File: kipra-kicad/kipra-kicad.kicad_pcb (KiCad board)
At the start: 2 copper layers, 128.2 x 134.8 mm, 51 parts

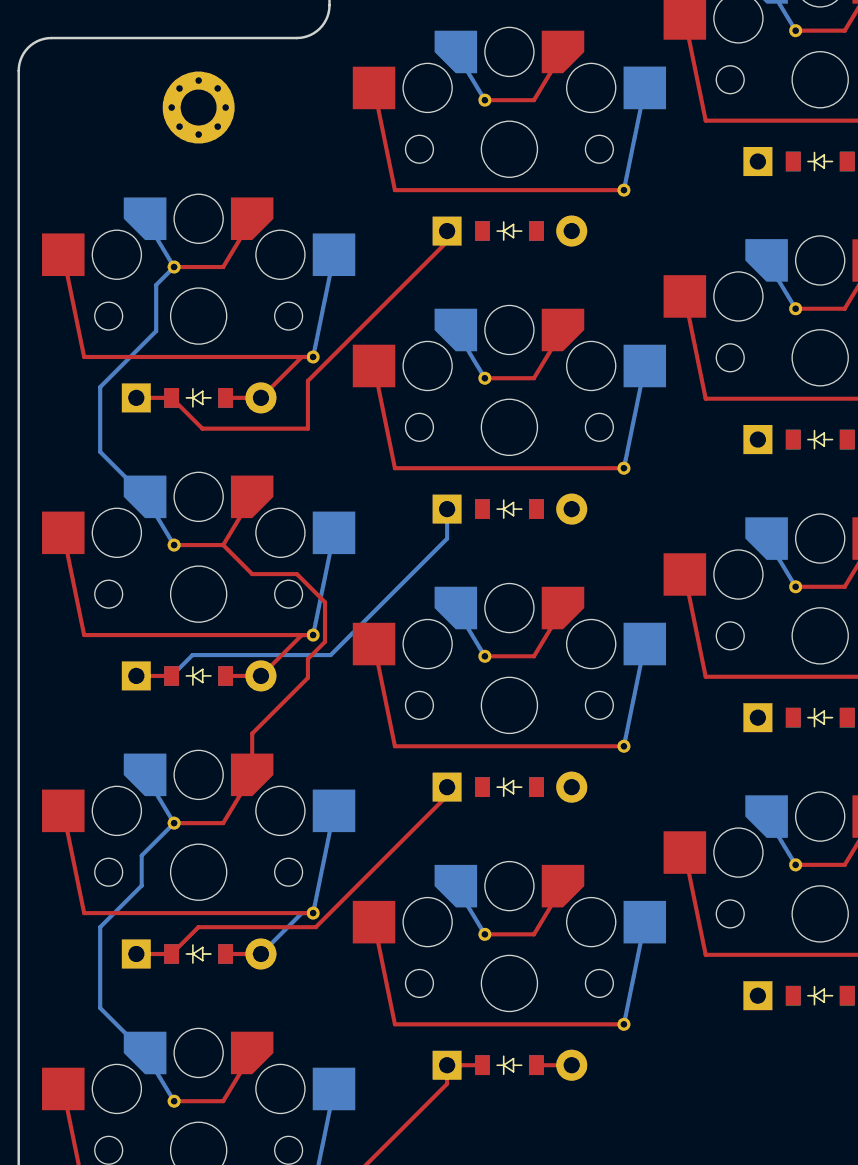
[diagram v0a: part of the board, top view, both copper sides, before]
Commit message: route traces up ring column
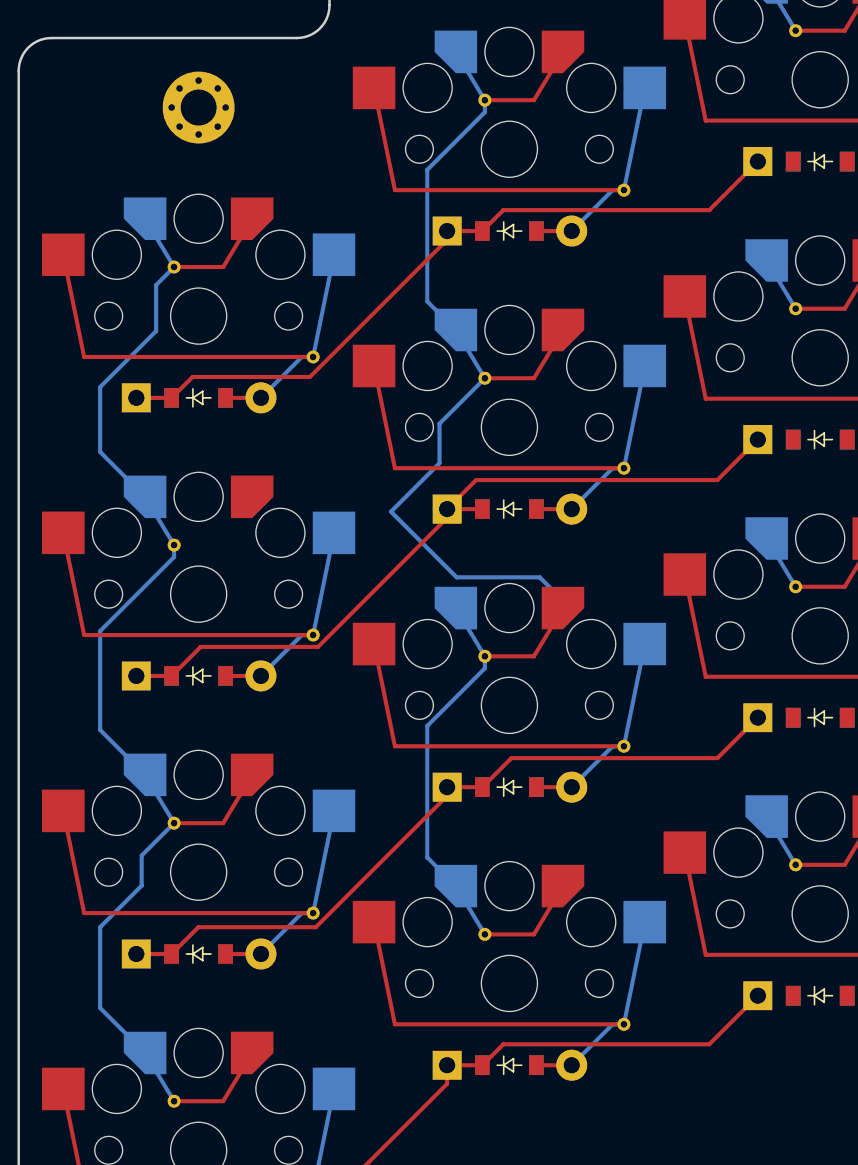
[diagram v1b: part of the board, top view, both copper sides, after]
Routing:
- net P16: track 49.7 -> 105.0 mm
- net P06: track 24.3 -> 46.5 mm
- net P07: track 23.5 -> 44.3 mm
- net P08: track 26.1 -> 44.7 mm
- net P05: track 26.9 -> 44.3 mm
- net P10: track 103.9 -> 94.5 mm
- net ring_two: track 26.8 -> 33.1 mm
- net ring_three: track 26.8 -> 33.1 mm
- net ring_four: track 26.8 -> 33.1 mm
- net ring_one: track 28.9 -> 33.1 mm
- net pinky_three: track 33.1 -> 33.8 mm
- net pinky_four: track 33.1 -> 33.8 mm

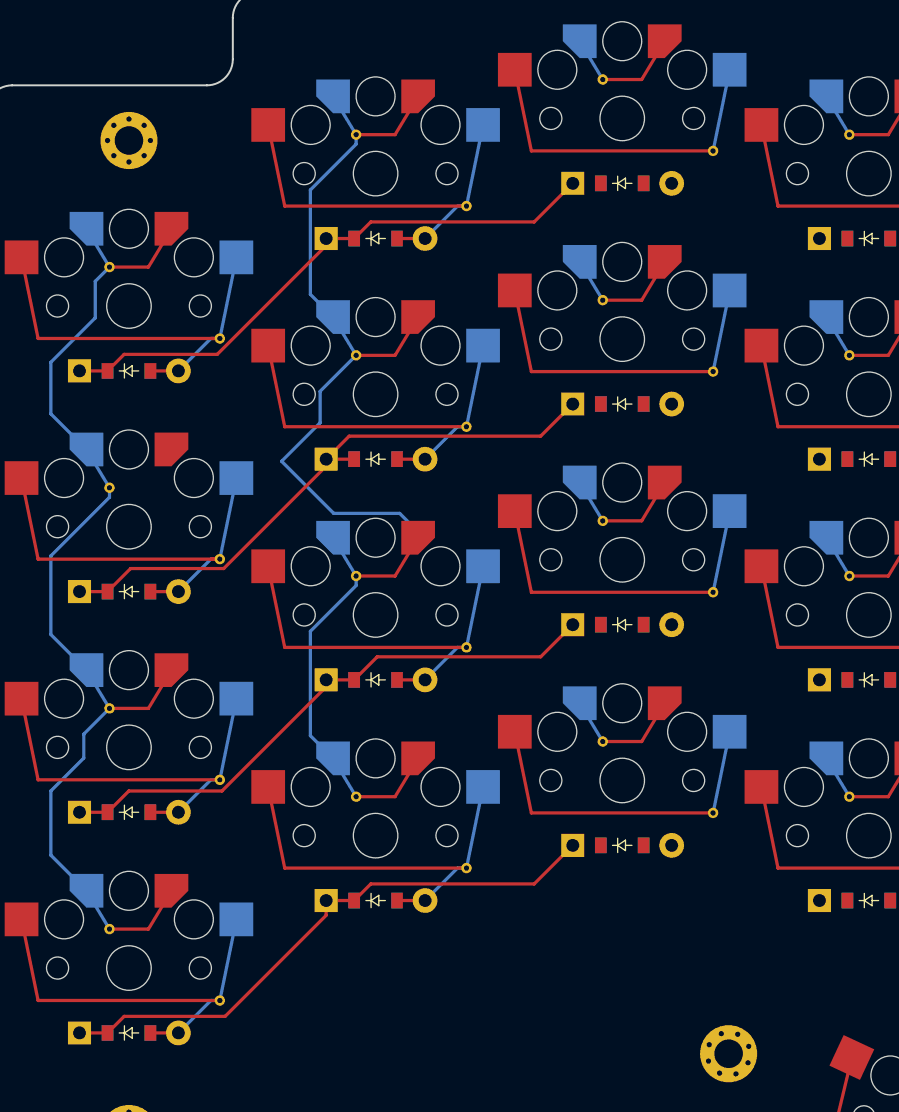
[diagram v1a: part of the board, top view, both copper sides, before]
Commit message: route traces up middle column
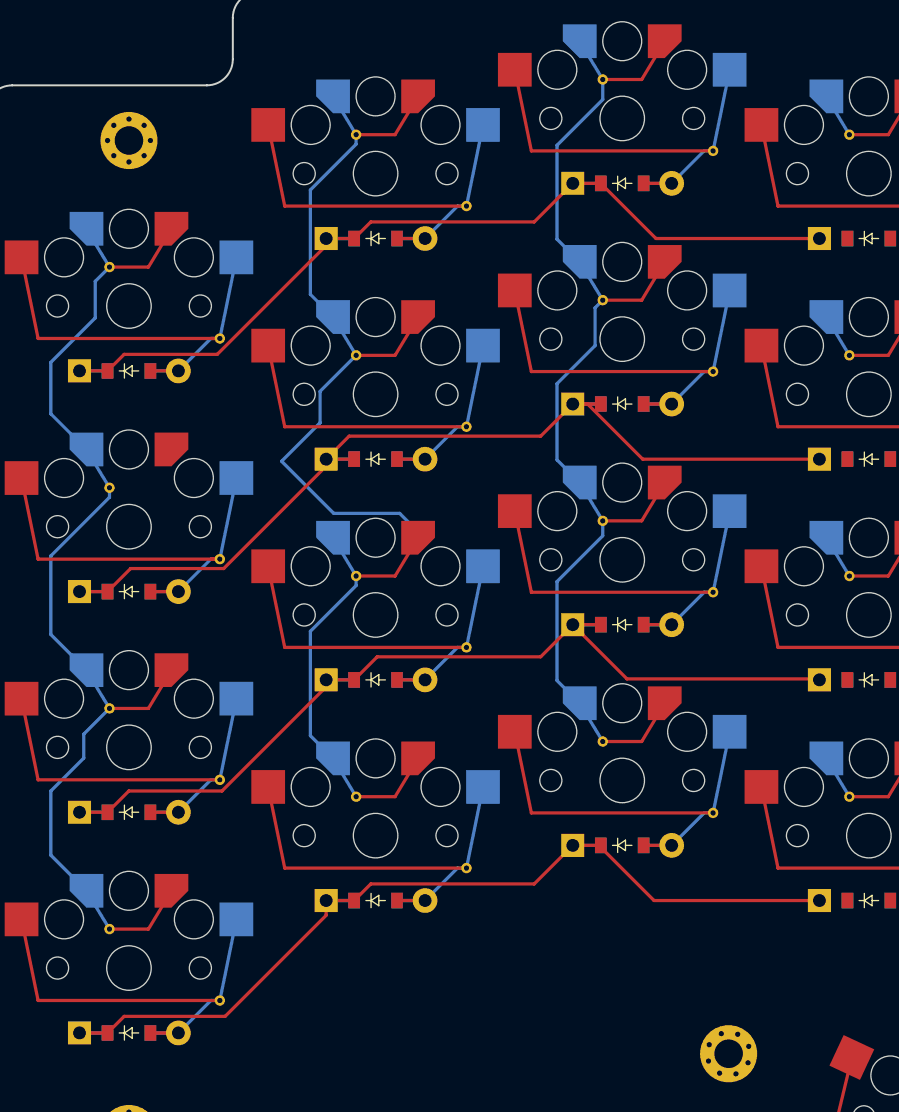
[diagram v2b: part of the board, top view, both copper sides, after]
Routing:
- net P14: track 49.7 -> 98.4 mm
- net P07: track 44.3 -> 73.7 mm
- net P06: track 46.5 -> 75.9 mm
- net P08: track 44.7 -> 72.0 mm
- net P05: track 44.3 -> 71.5 mm
- net middle_two: track 26.8 -> 35.3 mm
- net middle_three: track 26.8 -> 35.3 mm
- net middle_one: track 26.8 -> 35.3 mm
- net middle_four: track 26.8 -> 35.3 mm
- net ring_two: track 33.1 -> 35.3 mm
- net ring_three: track 33.1 -> 35.3 mm
- net ring_one: track 33.1 -> 35.3 mm
- net ring_four: track 33.1 -> 35.3 mm
- net pinky_two: track 33.1 -> 35.3 mm
- net pinky_three: track 33.8 -> 36.0 mm
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
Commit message: I think maybe I just need ground now
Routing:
- net P10: track 94.5 -> 257.1 mm
- net P19: track 39.8 -> 185.2 mm, vias 0 -> 1
- net P16: track 105.0 -> 221.0 mm
- net P15: track 49.7 -> 144.9 mm
- net P14: track 98.4 -> 193.4 mm
- net P06: track 75.9 -> 166.6 mm
- net P07: track 73.7 -> 156.7 mm, vias 0 -> 2
- net VCC: track 10.2 -> 87.7 mm
- net P08: track 72.0 -> 141.6 mm
- net P18: track 39.8 -> 95.6 mm
- net P3: track 10.2 -> 59.6 mm
- net P2: track 10.2 -> 57.8 mm
- net P05: track 71.5 -> 95.9 mm
- net thumb_near: track 26.8 -> 35.8 mm
- net thumb_middle: track 26.8 -> 35.5 mm
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
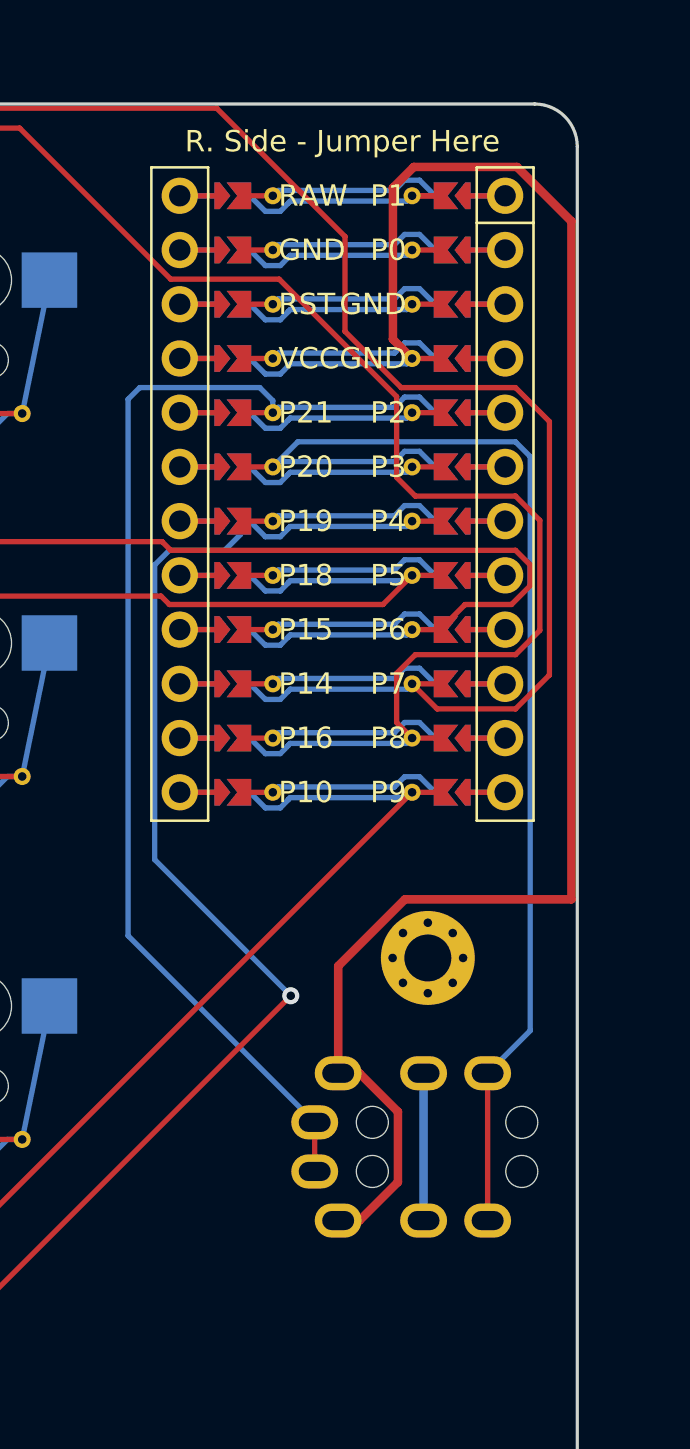
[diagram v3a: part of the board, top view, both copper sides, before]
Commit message: only DRC errors are GND filled zone issues
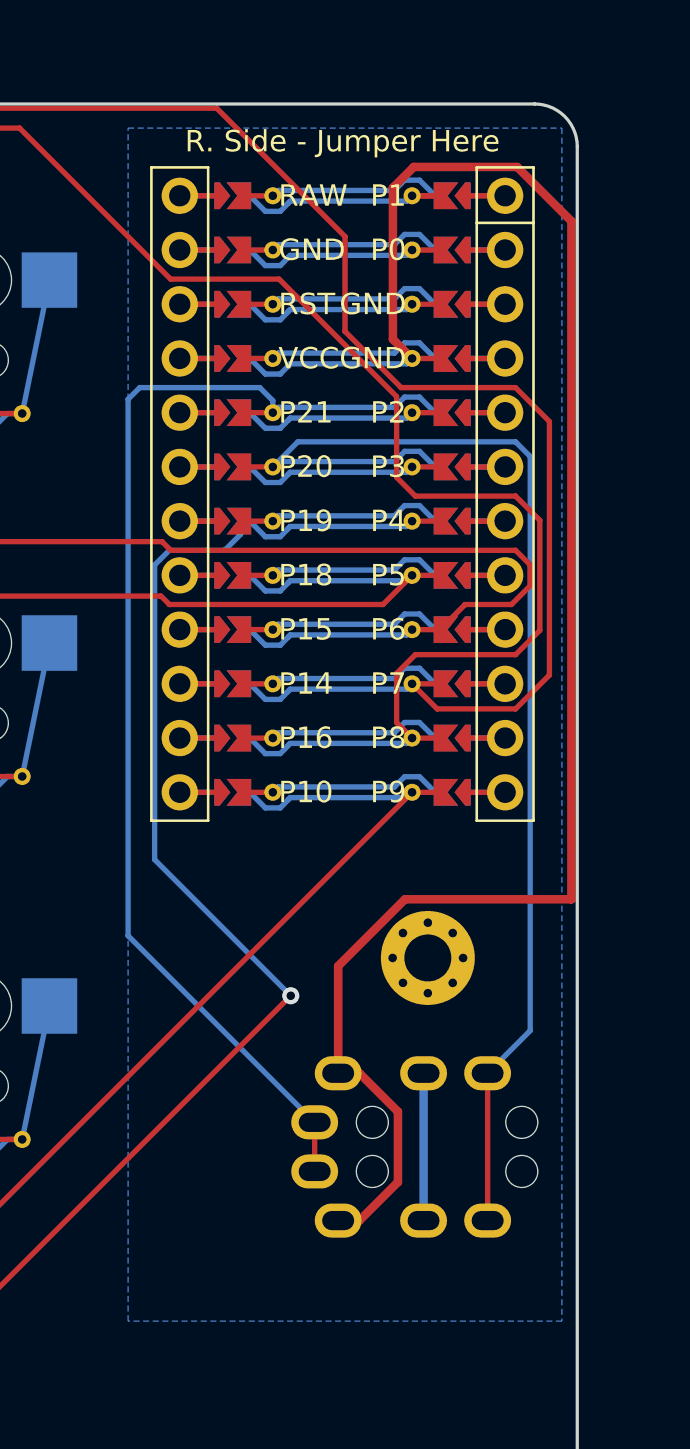
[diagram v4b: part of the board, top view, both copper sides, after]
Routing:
- added copper zone on B.Cu, net GND
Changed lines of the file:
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@@
   (segment (start 203.5 61.59) (end 205.62 61.59) (width 0.25) (layer "F.Cu") (net 72))
   (segment (start 205.62 61.59) (end 203.5 61.59) (width 0.25) (layer "B.Cu") (net 72))
+  (zone (net 34) (net_name "GND") (layer "B.Cu") (hatch edge 0.5)
+    (connect_pads (clearance 0.508))
+    (min_thickness 0.25) (filled_areas_thickness no)
+    (fill yes (thermal_gap 0.5) (thermal_bridge_width 0.5))
+    (polygon
+      (pts
+        (xy 187.96 30.48)
+        (xy 208.28 30.48)
+        (xy 208.28 86.36)
+        (xy 187.96 86.36)
+      )
+    )
+  )
 )

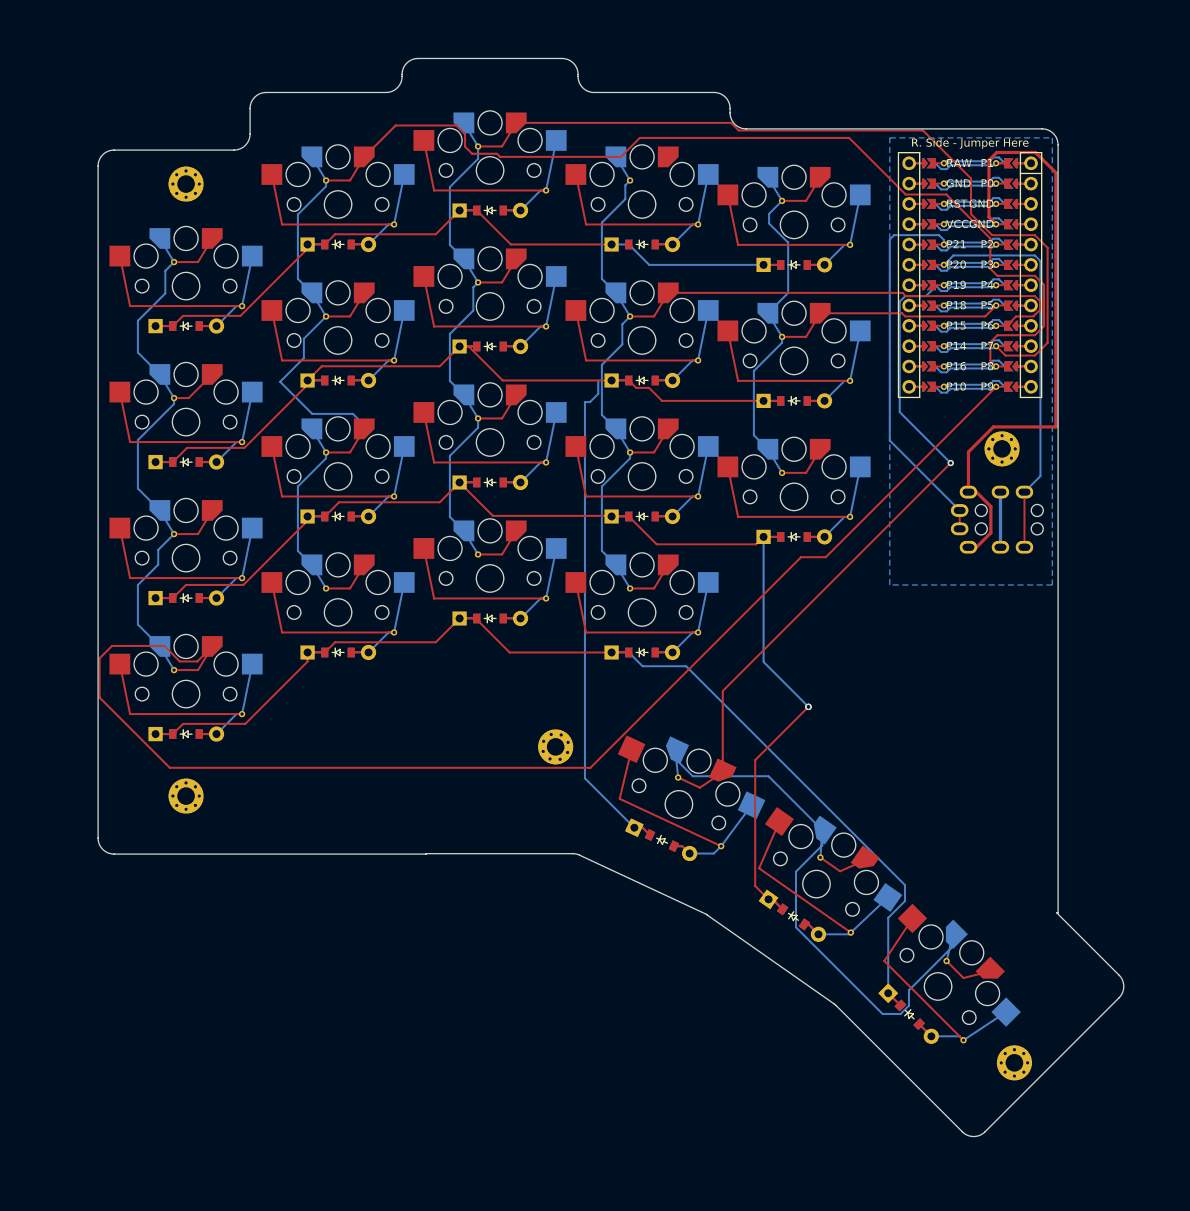
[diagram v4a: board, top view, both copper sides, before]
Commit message: all DRC errors fixed
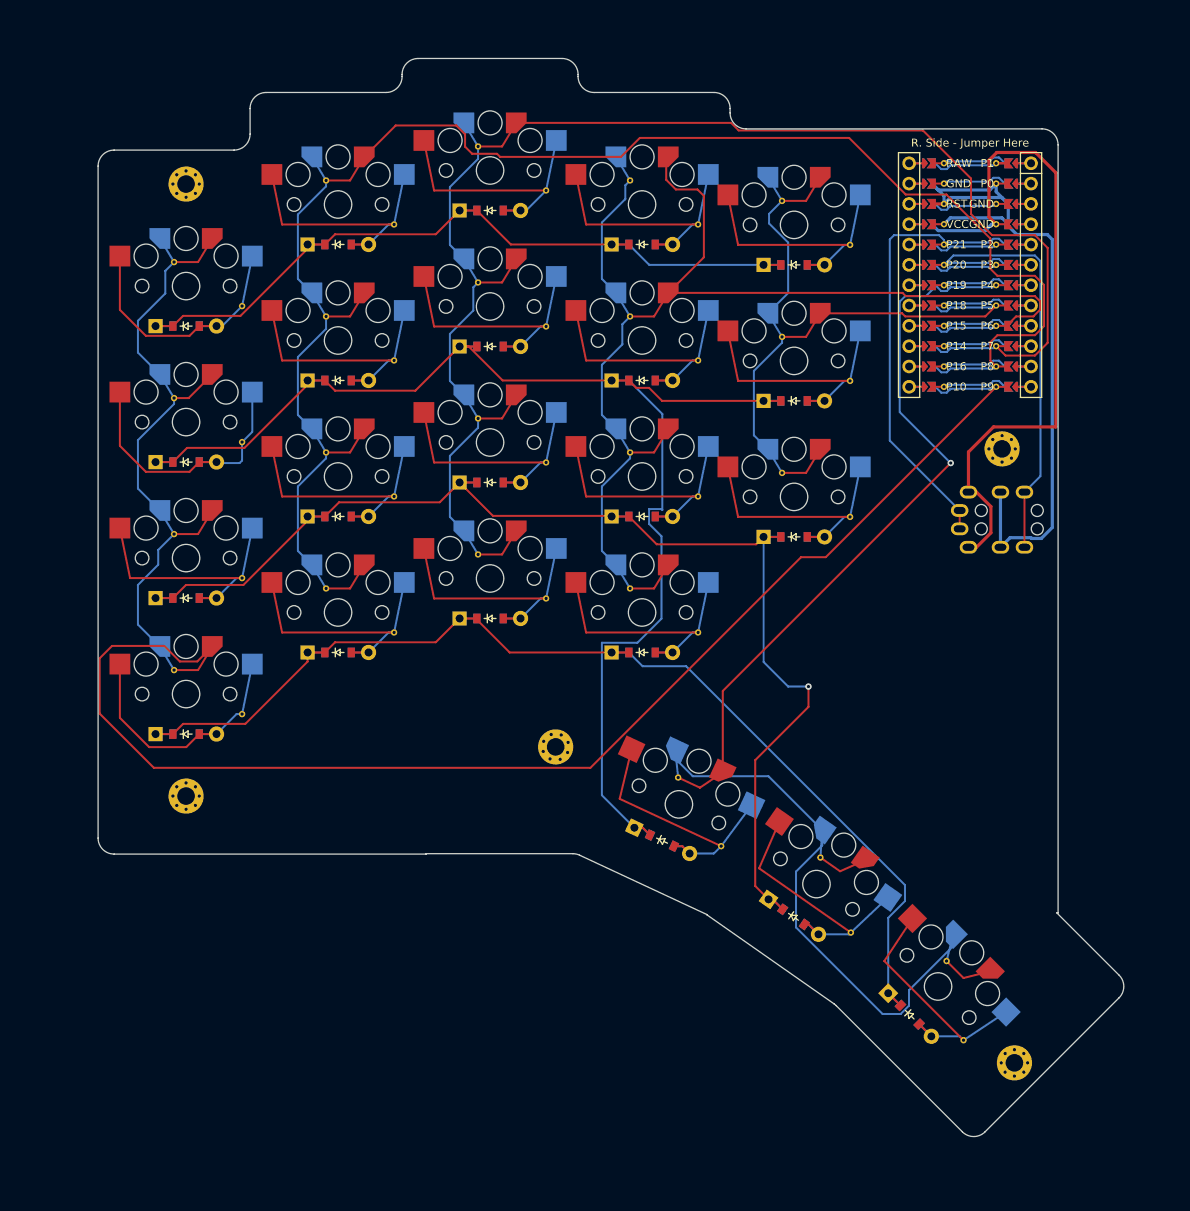
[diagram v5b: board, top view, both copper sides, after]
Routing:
- net GND: track 37.4 -> 96.4 mm
- net P15: track 144.9 -> 167.4 mm
- net P06: track 166.6 -> 173.4 mm
- net P16: track 221.0 -> 214.4 mm
- net P05: track 95.9 -> 98.1 mm
- net pinky_four: track 36.0 -> 34.2 mm
- net pinky_one: track 35.3 -> 33.8 mm
- net P07: track 156.7 -> 158.1 mm, vias 2 -> 1
- net P10: track 257.1 -> 258.3 mm
- net pinky_three: track 36.0 -> 35.4 mm
- removed copper zone on B.Cu, net GND
